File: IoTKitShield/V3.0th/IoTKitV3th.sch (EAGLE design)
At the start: 28 parts, among them J1 4P-2.0, J2 4P-2.0, J3 4P-2.0, J4 4p-2.54

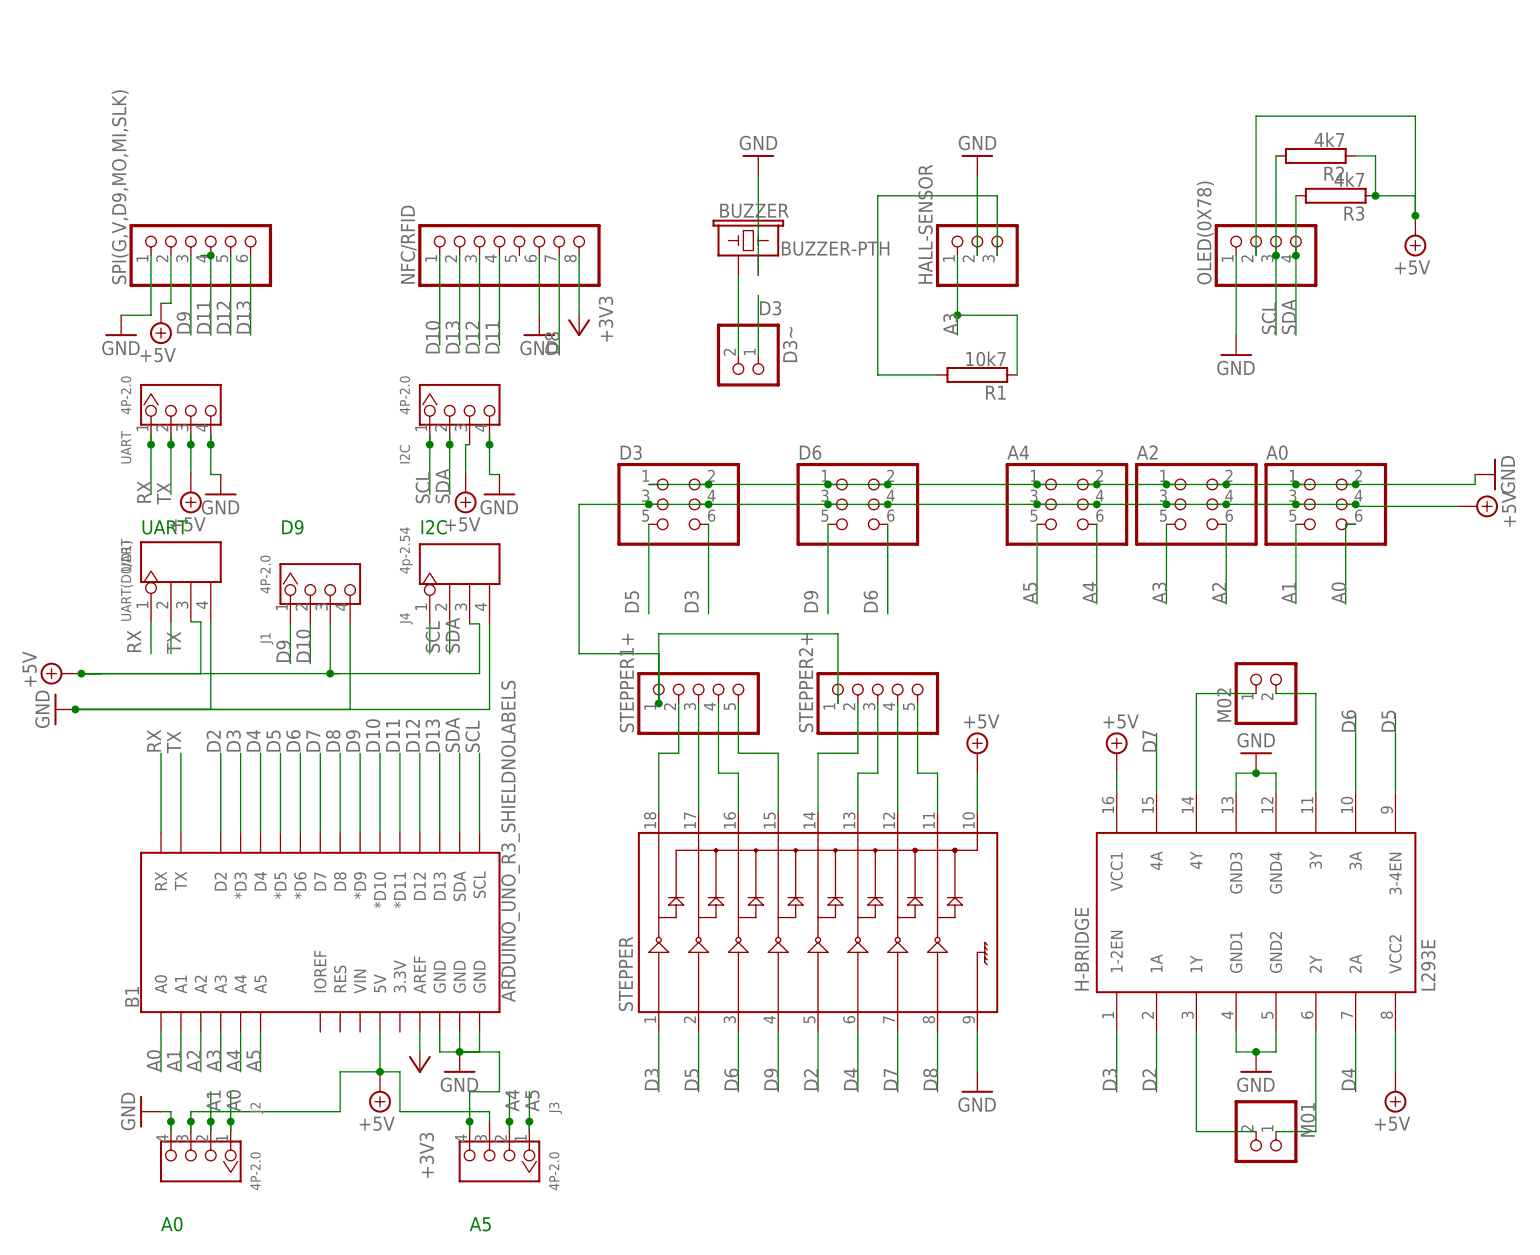
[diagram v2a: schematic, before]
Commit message: Korrekturen NFC, Hallsensor, Servos
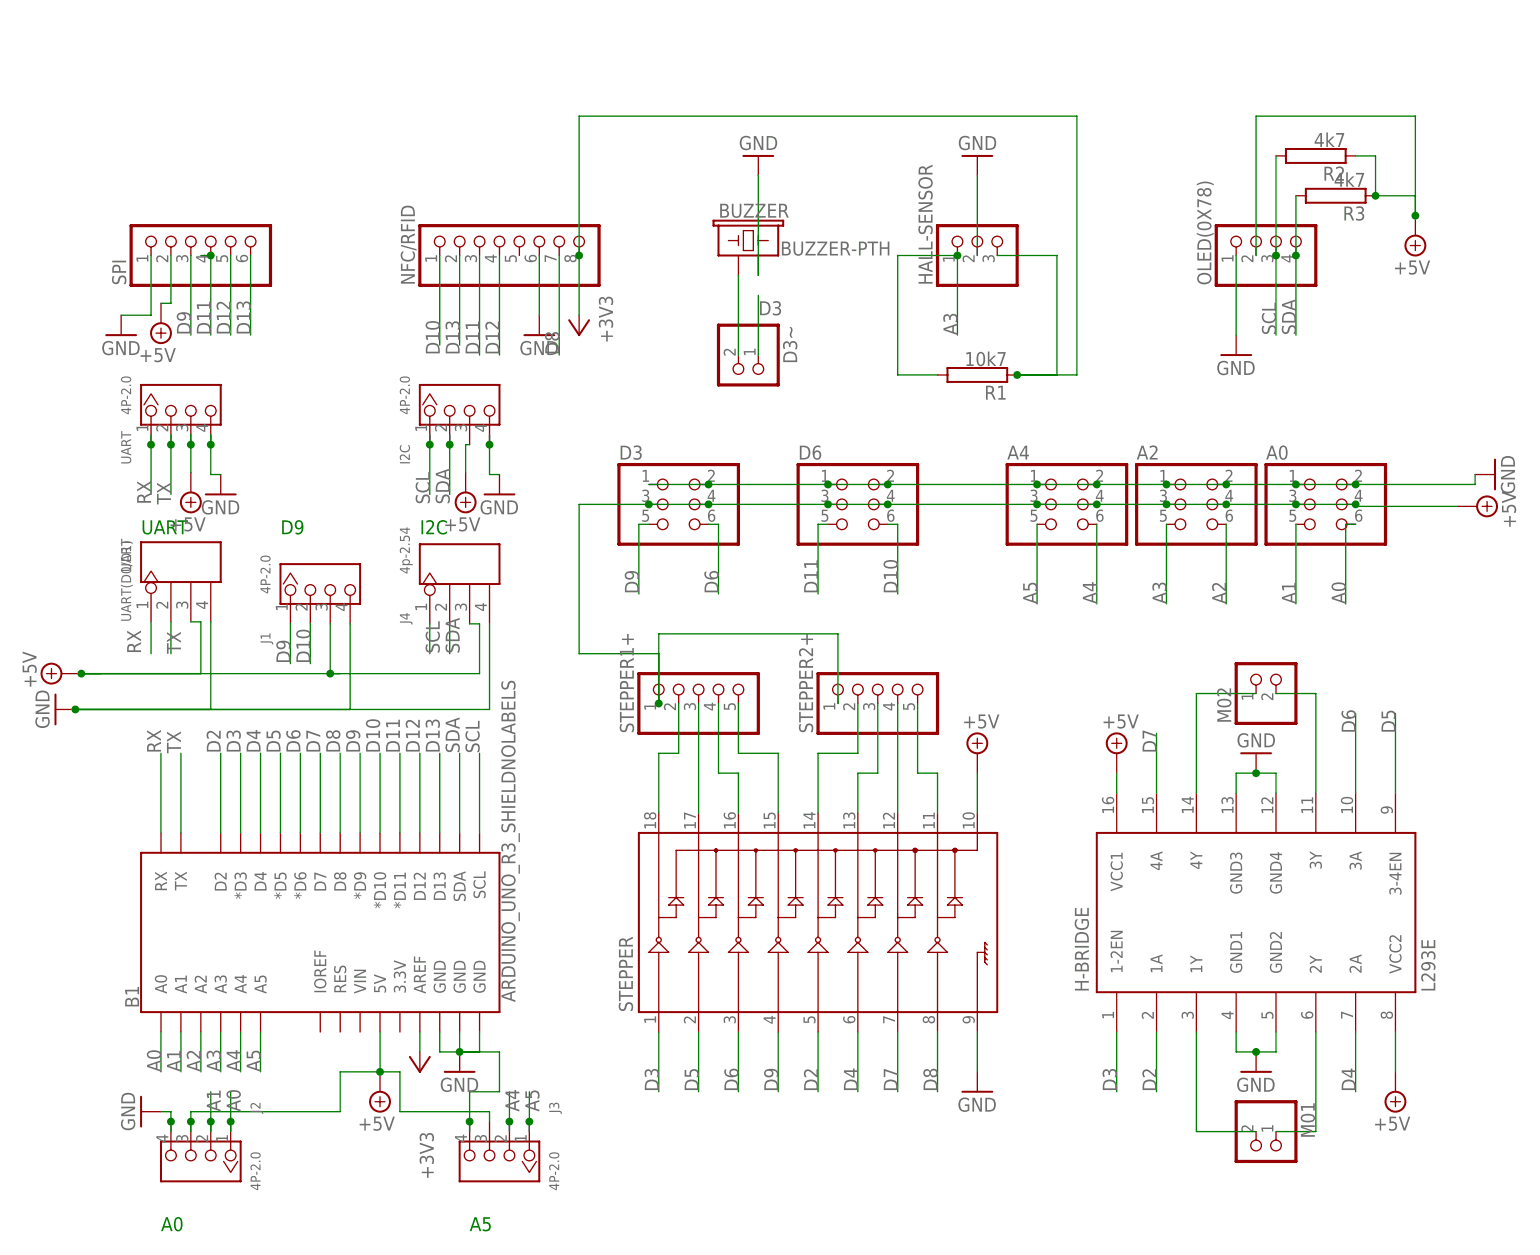
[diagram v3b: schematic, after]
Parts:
- renumbered SPI(G,V,D9,MO,MI,SLK) to SPI
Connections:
- removed net N$13: HALL-SENSOR.3, R1.2
- net +3V3: now also HALL-SENSOR.3, R1.1
- net A3: now also R1.2; no longer R1.1
- net D10: now also D6.6
- net D11: now also D6.5, NFC/RFID.3; no longer NFC/RFID.4
- net D12: now also NFC/RFID.4; no longer NFC/RFID.3
- net D3: no longer D3.6
- net D5: no longer D3.5
- net D6: now also D3.6; no longer D6.6
- net D9: now also D3.5; no longer D6.5
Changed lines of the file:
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@@
 <part name="A2" library="pinhead" deviceset="PINHD-2X3" device=""/>
 <part name="A0" library="pinhead" deviceset="PINHD-2X3" device=""/>
-<part name="SPI(G,V,D9,MO,MI,SLK)" library="pinhead" deviceset="PINHD-1X6" device=""/>
+<part name="SPI" library="pinhead" deviceset="PINHD-1X6" device=""/>
 <part name="NFC/RFID" library="pinhead" deviceset="PINHD-1X8" device=""/>
 <part name="HALL-SENSOR" library="pinhead" deviceset="PINHD-1X3" device=""/>
@@
 </instance>
 <instance part="D3" gate="A" x="69.85" y="92.71">
-<attribute name="NAME" x="63.5" y="98.425" size="1.778" layer="95"/>
 <attribute name="VALUE" x="63.5" y="85.09" size="1.778" layer="96"/>
 </instance>
 <instance part="D6" gate="A" x="92.71" y="92.71">
-<attribute name="NAME" x="86.36" y="98.425" size="1.778" layer="95"/>
 <attribute name="VALUE" x="86.36" y="85.09" size="1.778" layer="96"/>
 </instance>
@@
 <attribute name="VALUE" x="146.05" y="85.09" size="1.778" layer="96"/>
 </instance>
-<instance part="SPI(G,V,D9,MO,MI,SLK)" gate="A" x="11.43" y="127" rot="R90">
+<instance part="SPI" gate="A" x="11.43" y="127" rot="R90">
 <attribute name="NAME" x="0.635" y="120.65" size="1.778" layer="95" rot="R90"/>
 <attribute name="VALUE" x="21.59" y="120.65" size="1.778" layer="96" rot="R90"/>
@@
 </segment>
 <segment>
-<pinref part="D3" gate="A" pin="6"/>
-<wire x1="74.93" y1="90.17" x2="74.93" y2="78.74" width="0.1524" layer="91"/>
-<label x="73.66" y="78.74" size="1.778" layer="95" rot="R90"/>
-</segment>
-<segment>
 <pinref part="D3~" gate="G$1" pin="1"/>
 <wire x1="81.28" y1="111.76" x2="81.28" y2="119.38" width="0.1524" layer="91"/>
@@
 <label x="162.56" y="63.5" size="1.778" layer="95" rot="R90"/>
 </segment>
-<segment>
-<pinref part="D3" gate="A" pin="5"/>
-<wire x1="67.31" y1="90.17" x2="67.31" y2="78.74" width="0.1524" layer="91"/>
-<label x="66.04" y="78.74" size="1.778" layer="95" rot="R90"/>
-</segment>
 </net>
 <net name="D6" class="0">
@@
 </segment>
 <segment>
-<pinref part="D6" gate="A" pin="6"/>
-<wire x1="97.79" y1="90.17" x2="97.79" y2="78.74" width="0.1524" layer="91"/>
-<label x="96.52" y="78.74" size="1.778" layer="95" rot="R90"/>
+<pinref part="D3" gate="A" pin="6"/>
+<wire x1="74.93" y1="90.17" x2="76.2" y2="90.17" width="0.1524" layer="91"/>
+<wire x1="76.2" y1="90.17" x2="76.2" y2="81.28" width="0.1524" layer="91"/>
+<label x="76.2" y="81.28" size="1.778" layer="95" rot="R90"/>
 </segment>
 </net>
@@
 </segment>
 <segment>
-<pinref part="SPI(G,V,D9,MO,MI,SLK)" gate="A" pin="3"/>
+<pinref part="SPI" gate="A" pin="3"/>
 <wire x1="8.89" y1="124.46" x2="8.89" y2="114.3" width="0.1524" layer="91"/>
 <label x="8.89" y="114.3" size="1.778" layer="95" rot="R90"/>
 </segment>
 <segment>
-<pinref part="D6" gate="A" pin="5"/>
-<wire x1="90.17" y1="90.17" x2="90.17" y2="78.74" width="0.1524" layer="91"/>
-<label x="88.9" y="78.74" size="1.778" layer="95" rot="R90"/>
+<pinref part="D3" gate="A" pin="5"/>
+<wire x1="67.31" y1="90.17" x2="66.04" y2="90.17" width="0.1524" layer="91"/>
+<wire x1="66.04" y1="90.17" x2="66.04" y2="81.28" width="0.1524" layer="91"/>
+<label x="66.04" y="81.28" size="1.778" layer="95" rot="R90"/>
 </segment>
 </net>
@@
 <segment>
 <pinref part="HALL-SENSOR" gate="A" pin="1"/>
-<wire x1="106.68" y1="124.46" x2="106.68" y2="116.84" width="0.1524" layer="91"/>
+<wire x1="106.68" y1="124.46" x2="106.68" y2="114.3" width="0.1524" layer="91"/>
 <label x="106.68" y="114.3" size="1.778" layer="95" rot="R90"/>
-<pinref part="R1" gate="G$1" pin="1"/>
-<wire x1="106.68" y1="116.84" x2="106.68" y2="114.3" width="0.1524" layer="91"/>
-<wire x1="114.3" y1="109.22" x2="114.3" y2="116.84" width="0.1524" layer="91"/>
-<wire x1="114.3" y1="116.84" x2="106.68" y2="116.84" width="0.1524" layer="91"/>
-<junction x="106.68" y="116.84"/>
+<wire x1="106.68" y1="124.46" x2="99.06" y2="124.46" width="0.1524" layer="91"/>
+<junction x="106.68" y="124.46"/>
+<pinref part="R1" gate="G$1" pin="2"/>
+<wire x1="99.06" y1="124.46" x2="99.06" y2="109.22" width="0.1524" layer="91"/>
+<wire x1="99.06" y1="109.22" x2="104.14" y2="109.22" width="0.1524" layer="91"/>
 </segment>
 </net>
@@
 <label x="40.64" y="111.76" size="1.778" layer="95" rot="R90"/>
 </segment>
+<segment>
+<pinref part="D6" gate="A" pin="6"/>
+<wire x1="97.79" y1="90.17" x2="99.06" y2="90.17" width="0.1524" layer="91"/>
+<wire x1="99.06" y1="90.17" x2="99.06" y2="81.28" width="0.1524" layer="91"/>
+<label x="99.06" y="81.28" size="1.778" layer="95" rot="R90"/>
+</segment>
 </net>
 <net name="D11" class="0">
@@
 <wire x1="11.43" y1="124.46" x2="11.43" y2="114.3" width="0.1524" layer="91"/>
 <label x="11.43" y="114.3" size="1.778" layer="95" rot="R90"/>
-<pinref part="SPI(G,V,D9,MO,MI,SLK)" gate="A" pin="4"/>
+<pinref part="SPI" gate="A" pin="4"/>
 <junction x="11.43" y="124.46"/>
 </segment>
 <segment>
-<pinref part="NFC/RFID" gate="A" pin="4"/>
-<wire x1="48.26" y1="124.46" x2="48.26" y2="113.03" width="0.1524" layer="91"/>
-<label x="48.26" y="111.76" size="1.778" layer="95" rot="R90"/>
+<pinref part="NFC/RFID" gate="A" pin="3"/>
+<wire x1="45.72" y1="124.46" x2="45.72" y2="111.76" width="0.1524" layer="91"/>
+<label x="45.72" y="111.76" size="1.778" layer="95" rot="R90"/>
+</segment>
+<segment>
+<pinref part="D6" gate="A" pin="5"/>
+<wire x1="90.17" y1="90.17" x2="88.9" y2="90.17" width="0.1524" layer="91"/>
+<wire x1="88.9" y1="90.17" x2="88.9" y2="81.28" width="0.1524" layer="91"/>
+<label x="88.9" y="81.28" size="1.778" layer="95" rot="R90"/>
 </segment>
 </net>
@@
 </segment>
 <segment>
-<pinref part="SPI(G,V,D9,MO,MI,SLK)" gate="A" pin="5"/>
+<pinref part="SPI" gate="A" pin="5"/>
 <wire x1="13.97" y1="124.46" x2="13.97" y2="114.3" width="0.1524" layer="91"/>
 <label x="13.97" y="114.3" size="1.778" layer="95" rot="R90"/>
 </segment>
 <segment>
-<pinref part="NFC/RFID" gate="A" pin="3"/>
-<wire x1="45.72" y1="124.46" x2="45.72" y2="113.03" width="0.1524" layer="91"/>
-<label x="45.72" y="111.76" size="1.778" layer="95" rot="R90"/>
+<pinref part="NFC/RFID" gate="A" pin="4"/>
+<wire x1="48.26" y1="124.46" x2="48.26" y2="111.76" width="0.1524" layer="91"/>
+<label x="48.26" y="111.76" size="1.778" layer="95" rot="R90"/>
 </segment>
 </net>
@@
 </segment>
 <segment>
-<pinref part="SPI(G,V,D9,MO,MI,SLK)" gate="A" pin="6"/>
+<pinref part="SPI" gate="A" pin="6"/>
 <wire x1="16.51" y1="124.46" x2="16.51" y2="114.3" width="0.1524" layer="91"/>
 <label x="16.51" y="114.3" size="1.778" layer="95" rot="R90"/>
@@
 <junction x="147.32" y="124.46"/>
 <label x="147.32" y="114.3" size="1.778" layer="95" rot="R90"/>
-</segment>
-</net>
-<net name="N$13" class="0">
-<segment>
-<pinref part="R1" gate="G$1" pin="2"/>
-<wire x1="104.14" y1="109.22" x2="96.52" y2="109.22" width="0.1524" layer="91"/>
-<wire x1="96.52" y1="109.22" x2="96.52" y2="132.08" width="0.1524" layer="91"/>
-<wire x1="96.52" y1="132.08" x2="111.76" y2="132.08" width="0.1524" layer="91"/>
-<pinref part="HALL-SENSOR" gate="A" pin="3"/>
-<wire x1="111.76" y1="132.08" x2="111.76" y2="124.46" width="0.1524" layer="91"/>
 </segment>
 </net>
@@
 </segment>
 <segment>
-<pinref part="SPI(G,V,D9,MO,MI,SLK)" gate="A" pin="2"/>
+<pinref part="SPI" gate="A" pin="2"/>
 <pinref part="SUPPLY9" gate="+5V" pin="+5V"/>
 <wire x1="6.35" y1="124.46" x2="6.35" y2="118.364" width="0.1524" layer="91"/>
@@
 </segment>
 <segment>
-<pinref part="SPI(G,V,D9,MO,MI,SLK)" gate="A" pin="1"/>
+<pinref part="SPI" gate="A" pin="1"/>
 <pinref part="GND6" gate="1" pin="GND"/>
 <wire x1="3.81" y1="124.46" x2="3.81" y2="116.84" width="0.1524" layer="91"/>
@@
 <pinref part="+3V2" gate="G$1" pin="+3V3"/>
 <wire x1="58.42" y1="124.46" x2="58.42" y2="116.84" width="0.1524" layer="91"/>
-</segment>
-<segment>
+<wire x1="58.42" y1="124.46" x2="58.42" y2="142.24" width="0.1524" layer="91"/>
+<junction x="58.42" y="124.46"/>
+<wire x1="58.42" y1="142.24" x2="121.92" y2="142.24" width="0.1524" layer="91"/>
+<wire x1="121.92" y1="142.24" x2="121.92" y2="109.22" width="0.1524" layer="91"/>
+<pinref part="R1" gate="G$1" pin="1"/>
+<wire x1="121.92" y1="109.22" x2="114.3" y2="109.22" width="0.1524" layer="91"/>
+<wire x1="114.3" y1="109.22" x2="119.38" y2="109.22" width="0.1524" layer="91"/>
+<junction x="114.3" y="109.22"/>
+<pinref part="HALL-SENSOR" gate="A" pin="3"/>
+<wire x1="119.38" y1="109.22" x2="119.38" y2="124.46" width="0.1524" layer="91"/>
+<wire x1="119.38" y1="124.46" x2="111.76" y2="124.46" width="0.1524" layer="91"/>
+</segment>
+<segment>
